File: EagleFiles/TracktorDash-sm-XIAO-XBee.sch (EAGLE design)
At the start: 11 parts

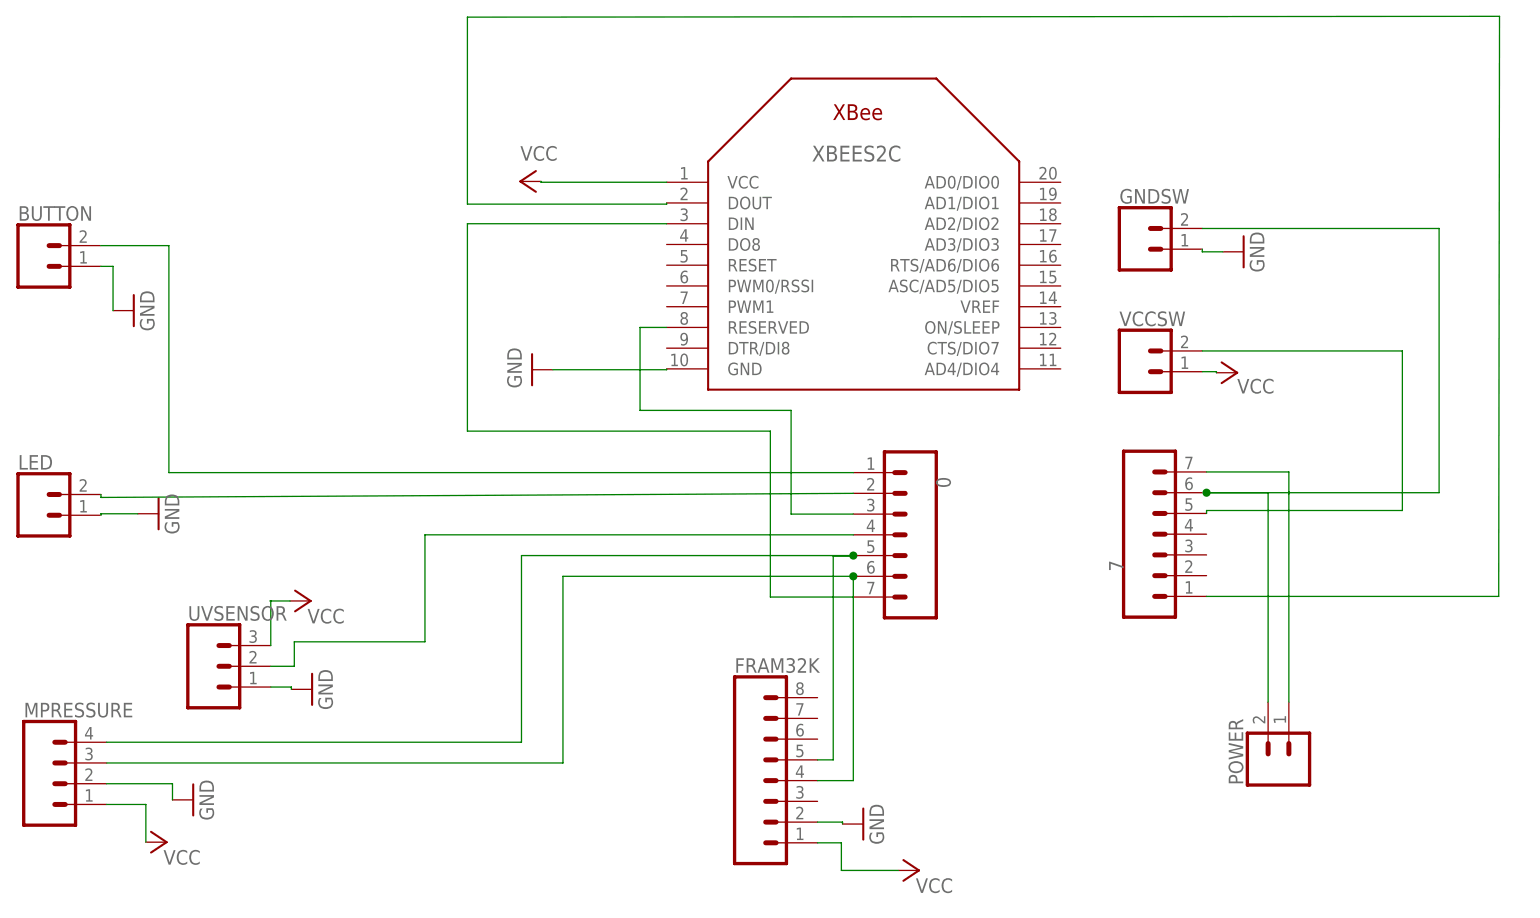
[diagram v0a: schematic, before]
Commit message: 2ND ORDER PCBWAY
FRAM ORIANTATION AND CONNECTIONS FIXED
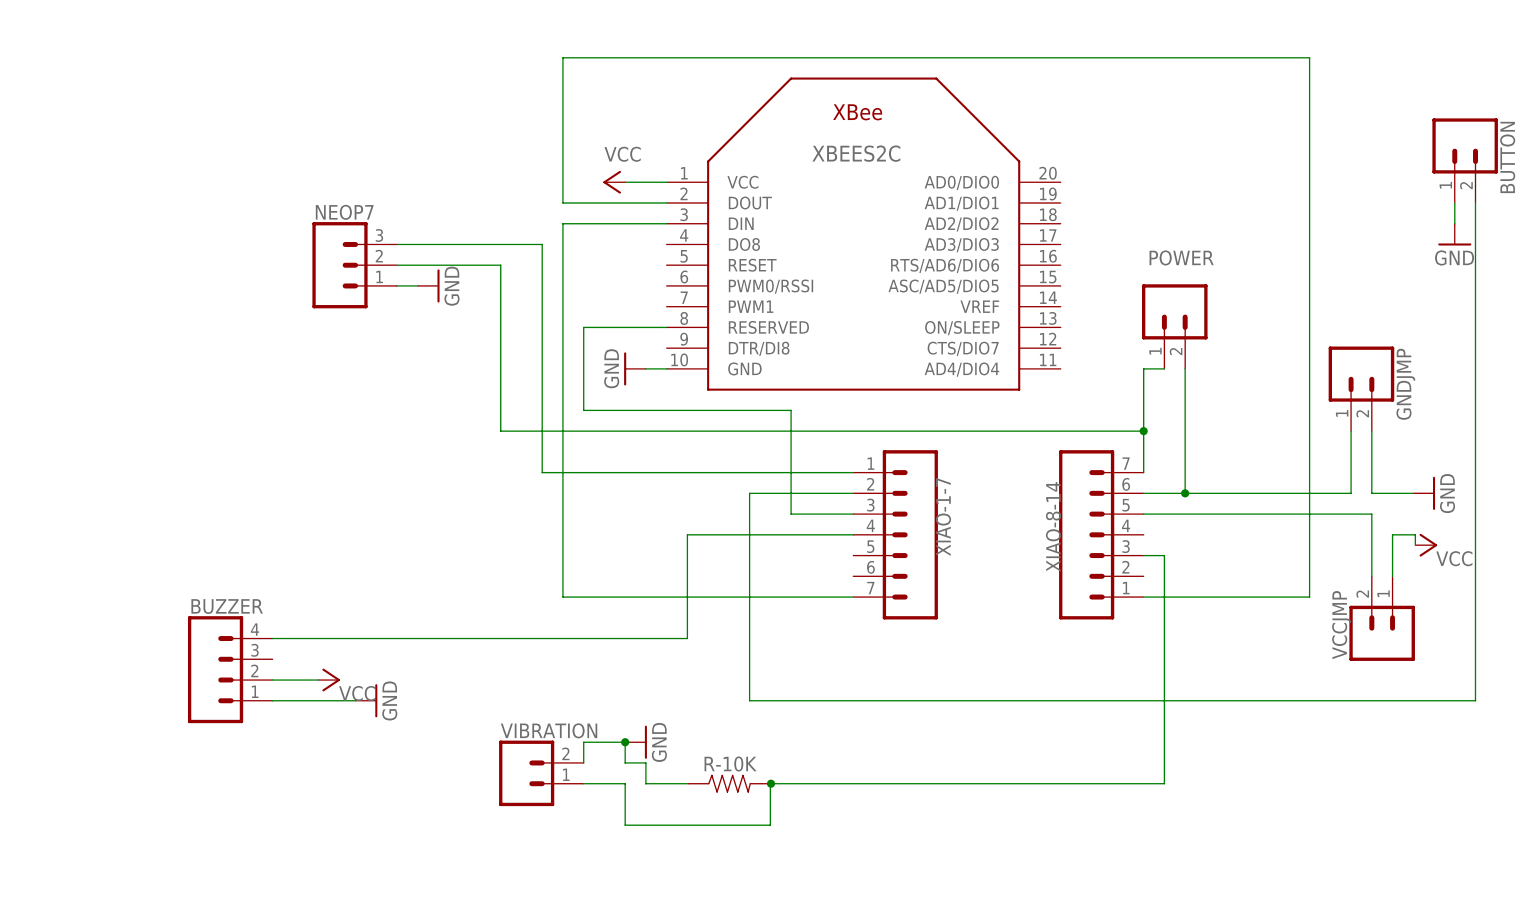
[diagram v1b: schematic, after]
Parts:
- removed 7: (no value), SparkFun-Connectors:CONN_07
- removed FRAM32K: FRAM32K, SparkFun-Connectors:CONN_08"
- removed GNDSW, VCCSW: button, SparkFun-Connectors:CONN_02
- removed LED: LED, SparkFun-Connectors:CONN_02
- removed MPRESSURE: (no value), SparkFun-Connectors:CONN_04PTH
- removed UVSENSOR: UV, SparkFun-Connectors:CONN_03
- added BUZZER: (no value), SparkFun-Connectors:CONN_041X04_NO_SILK
- added GNDJMP, VCCJMP, VIBRATION: (no value), SparkFun-Connectors:CONN_02
- added NEOP7: 455-1750-1-ND, SparkFun-Connectors:CONN_03
- added R-10K: 10, SparkFun-Resistors:10OHM-HORIZ-1/4W-1%
- added XIAO-8-14: (no value), SparkFun-Connectors:CONN_07
- POWER: value button -> (none)
- renumbered 0 to XIAO-1-7
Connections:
- removed net N$10: 7.5, VCCSW.2
- removed net N$7: BUTTON.2, XIAO-1-7.1
- new net N$12: GNDJMP.1, POWER.2, XIAO-8-14.6
- net GND: now also BUZZER.1, GNDJMP.2, NEOP7.1, R-10K.1, VIBRATION.2; no longer FRAM32K.2, GNDSW.1, LED.1, MPRESSURE.2, UVSENSOR.1
- net N$1: now also NEOP7.3, XIAO-1-7.1; no longer FRAM32K.5, MPRESSURE.4, XIAO-1-7.5
- net N$11: now also R-10K.2, VIBRATION.1, XIAO-8-14.3; no longer 7.7, POWER.1
- net N$2: now also VCCJMP.2, XIAO-8-14.5; no longer FRAM32K.4, MPRESSURE.3, XIAO-1-7.6
- net N$4: now also BUTTON.2, XIAO-1-7.2; no longer 7.6, GNDSW.2, POWER.2
- net N$6: now also BUZZER.4; no longer UVSENSOR.2
- net N$8: now also NEOP7.2, POWER.1, XIAO-8-14.7; no longer LED.2, XIAO-1-7.2
- net N$9: now also XIAO-8-14.1; no longer 7.1
- net VCC: now also BUZZER.2, VCCJMP.1; no longer FRAM32K.1, MPRESSURE.1, UVSENSOR.3, VCCSW.1
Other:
- moved on the sheet: BUTTON, POWER
